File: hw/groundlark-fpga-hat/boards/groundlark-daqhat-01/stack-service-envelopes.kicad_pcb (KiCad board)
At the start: 6 copper layers, 140 x 56 mm, 207 parts, among them J1 Raspberry Pi 40-pin, J130 PI BATTERY 8-18V, J131 SWD / 3V3 REF, J140 GNSS ANT / 3V3, J4 FPGA test UART/reset, J80 LSHM-150-04.0-L-DV-A-S-K-TR, J81 LSHM-150-04.0-L-DV-A-S-K-TR, J82 LSHM-130-04.0-L-DV-A-S-K-TR, J83 12V DC / CENTER +, J90 GEO + / - / SHIELD, Q1 2N7002, Q130 2N7002, Q131 2N7002, SW80 FPGA OFF / ON, U1 24LC32A, U100 TMUX1574PWR, U101 TMUX1574PWR, U102 TCA9534PWR, U103 SN74LVC1G10DCKR, U104 TLV809EA30DBZR, U105 TLV809EA30DBZR, U106 SN74LVC1G08DCKR, U11 LSM6DSOTR, U12 LSM6DSOTR, U13 LSM6DSOTR, U130 MSPM0L1106, U131 TPS70933, U132 TPSM53603, U133 TPS22953, U140 TPS70933, U141 TPS2553, U21 MAX-M10S-00B, U22 ADS122C04, U23 DLVR-F50D, U40 TLV1117LV33DCYR, U41 SN74LVC8T245PWR, U42 SN74LVC8T245PWR, U43 ISO1640BDR, U51 TXU0202DCUR, U52 TLV803EA30DBZR, U80 TPSM53603

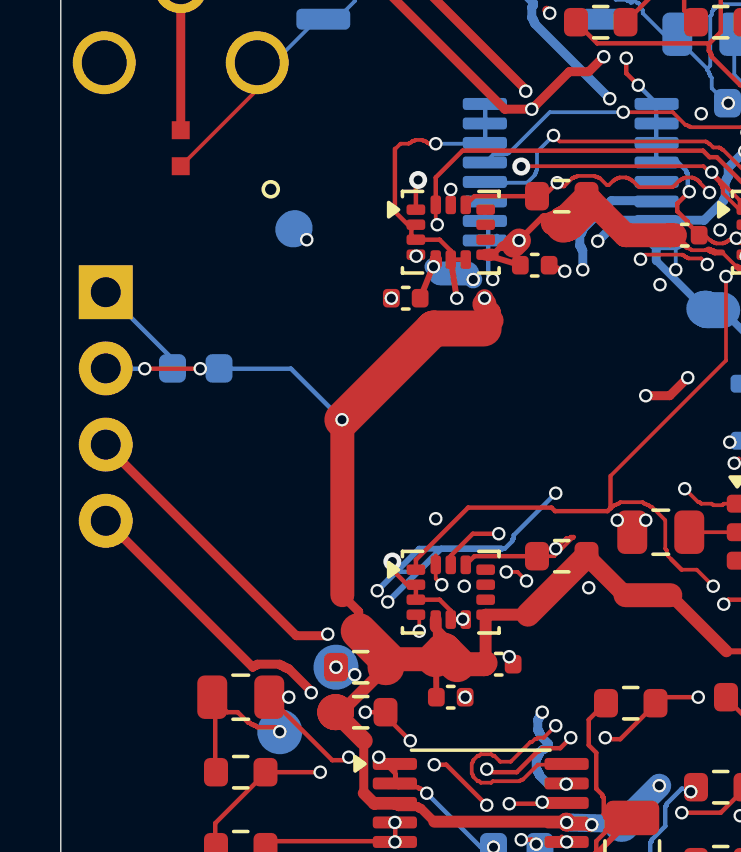
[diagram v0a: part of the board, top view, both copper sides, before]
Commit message: Update DAQHAT pressure sensor and assembly sourcing
Replace D90 with TPD2E2U06QDCKRQ1 and redesign U23 around SDP32-125PA. Synchronize routed CAD, native SES, models, supplier records, acquisition drivers, contracts, simulations, tests and documentation.

Record dated stock checks for 71 catalog identities and preserve the release gate for 52 unverified supplier placements. Generated manufacturing packages remain local and ignored.

Validation: repository structure and diff checks pass; prior full lab run passed 25 of 26 stages, with 301 software tests and 221 of 222 hardware tests passing. The remaining hardware test blocks unverified placements. Browser interaction and physical qualification remain pending.
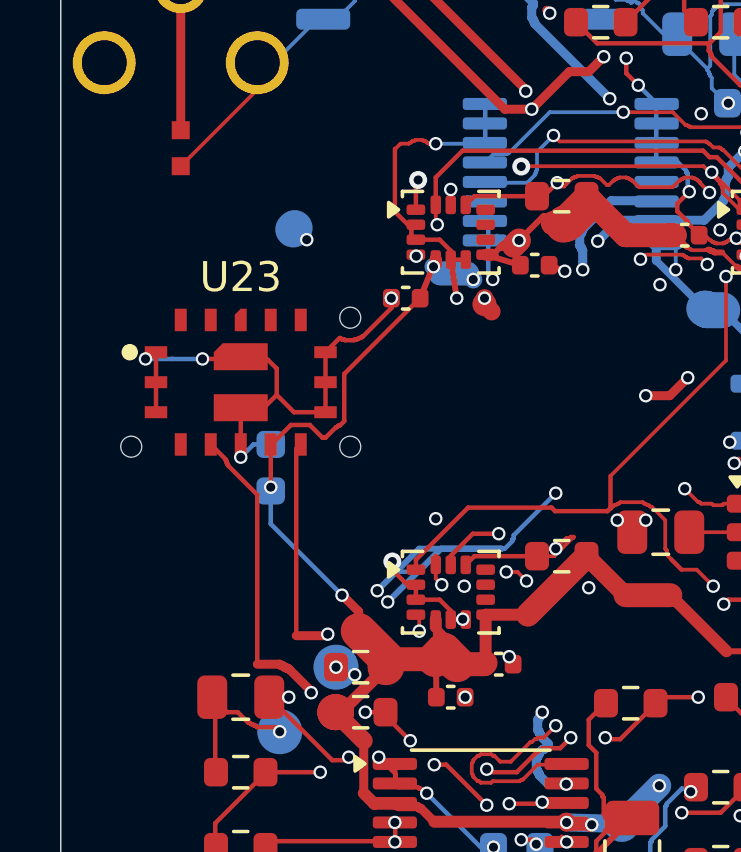
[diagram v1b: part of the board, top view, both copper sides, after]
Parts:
- U23: value DLVR-F50D -> SDP32-125PA; footprint Groundlark:Groundlark__DLVR_E1BS -> Groundlark:Groundlark__SDP32
- moved U23 5.41 mm to (56.0, 79.0), turned to 0 degrees
- moved C24 4.15 mm to (57.0, 81.8), turned to 90 degrees
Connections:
- U23 pad 2: SENS_3V3 -> GND
- U23 pad 3: I2C_SDA -> GND
- U23 pad 4: I2C_SCL -> PRESSURE_NC_4
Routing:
- net GND: track 671.4 -> 687.1 mm, vias 148 -> 151
- net SENS_3V3: track 250.1 -> 243.3 mm, vias 42 -> 41
- net I2C_SDA: track 66.7 -> 64.1 mm
- net I2C_SCL: track 85.0 -> 85.9 mm

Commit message: Strengthen DAQHAT power copper and validate native layout
Extend Pi supply pours to J1, add output via arrays and an FPGA distribution
bridge, spread D130 heat, correct GNSS RF width, and add UART idle bias.
Synchronize circuit, native CAD, schematic, SES, models and assembly mapping.

Extract native DC resistance, screen adjacent-layer coupling, preserve checks
under Python optimization, and disable I2C/I3C on the shared SPI IMUs.
Refresh specifications, supplier identity records and validation evidence.

Native ERC/DRC, route replay, simulations and 302 software tests pass. The final
hardware run passes 234/235; 52 supplier placement holds still prevent release.
All 71 exact catalog identities passed a fresh public inventory check.
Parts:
- added R118: 10k, Groundlark:Resistor_SMD__R_0603_1608Metric, F.Cu at (66.5, 65.1)
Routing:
- net PI_UART_RX: track 13.9 -> 21.0 mm, vias 2 -> 3
- net PI_3V3: track 320.2 -> 321.6 mm
- net PI_5V: vias 15 -> 29
- net FPGA_VIN: vias 17 -> 23
- net BAT_PROTECTED: vias 2 -> 11
- added copper zone on B.Cu, net BAT_PROTECTED
- added copper zone on F.Cu, net BAT_PROTECTED
- added copper zone on B.Cu, net PI_5V
- added copper zone on F.Cu, net PI_5V
